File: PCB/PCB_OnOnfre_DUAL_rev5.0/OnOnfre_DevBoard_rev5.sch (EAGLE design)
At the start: 30 parts, among them J3Y S8050, J7 8p, K1 OMRON-G3MB-202P-SSR2, K2 OMRON-G3MB-202P-SSR2, U2 esp12

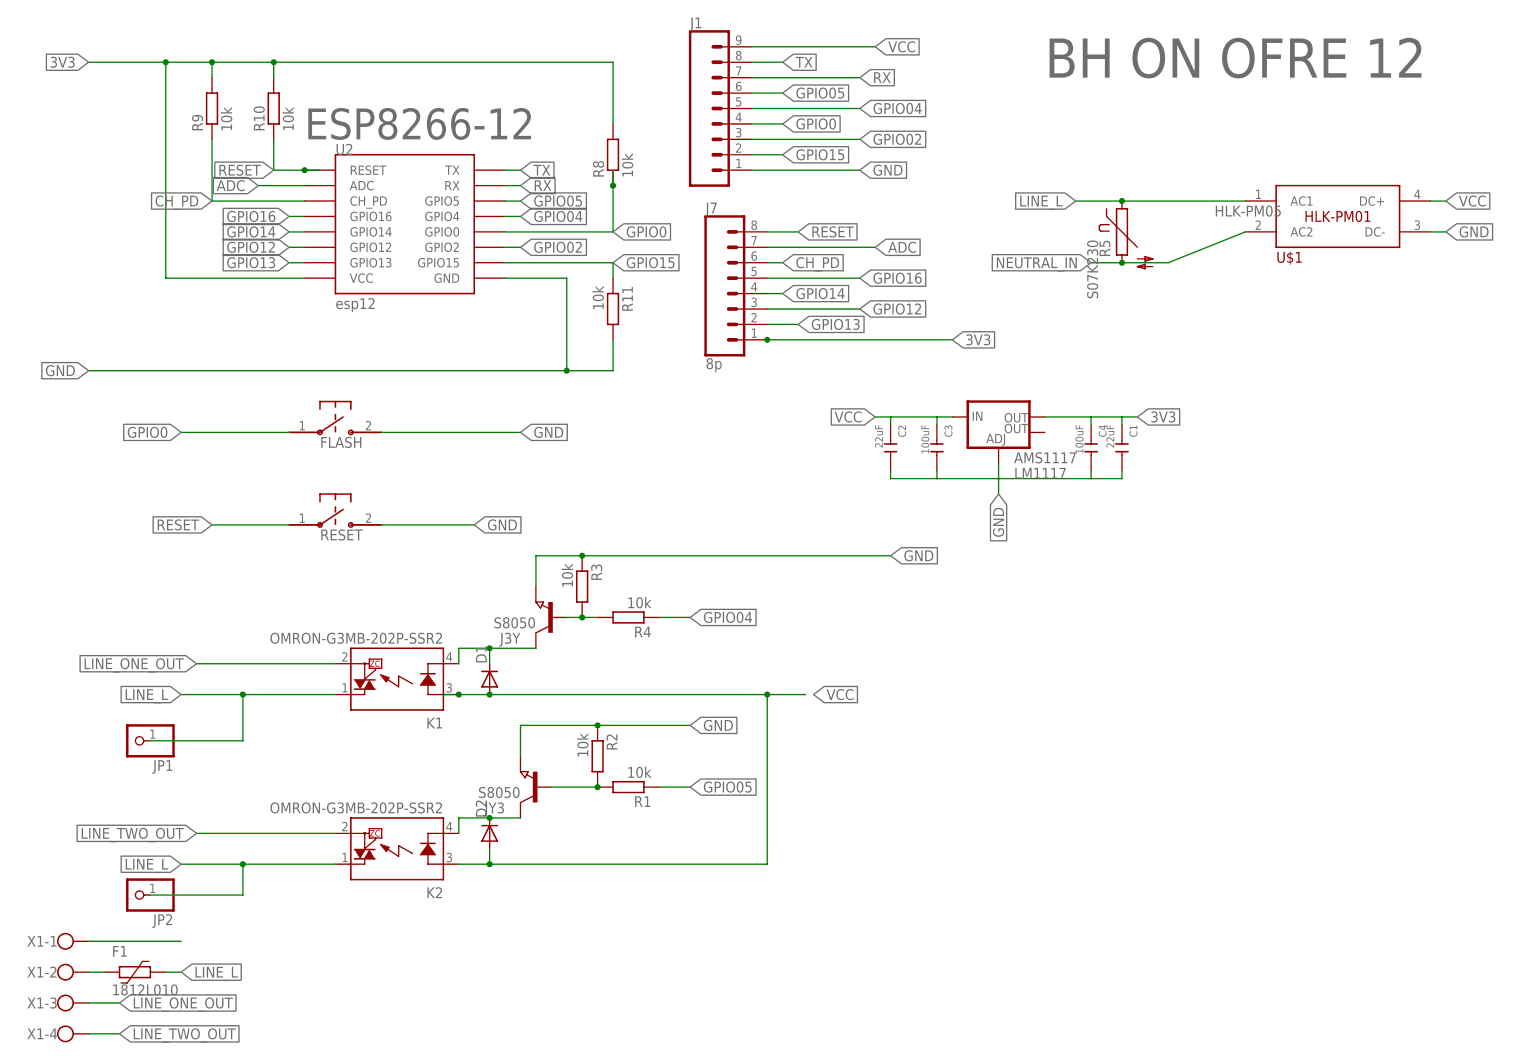
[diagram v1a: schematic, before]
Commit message: rev5 adc A0
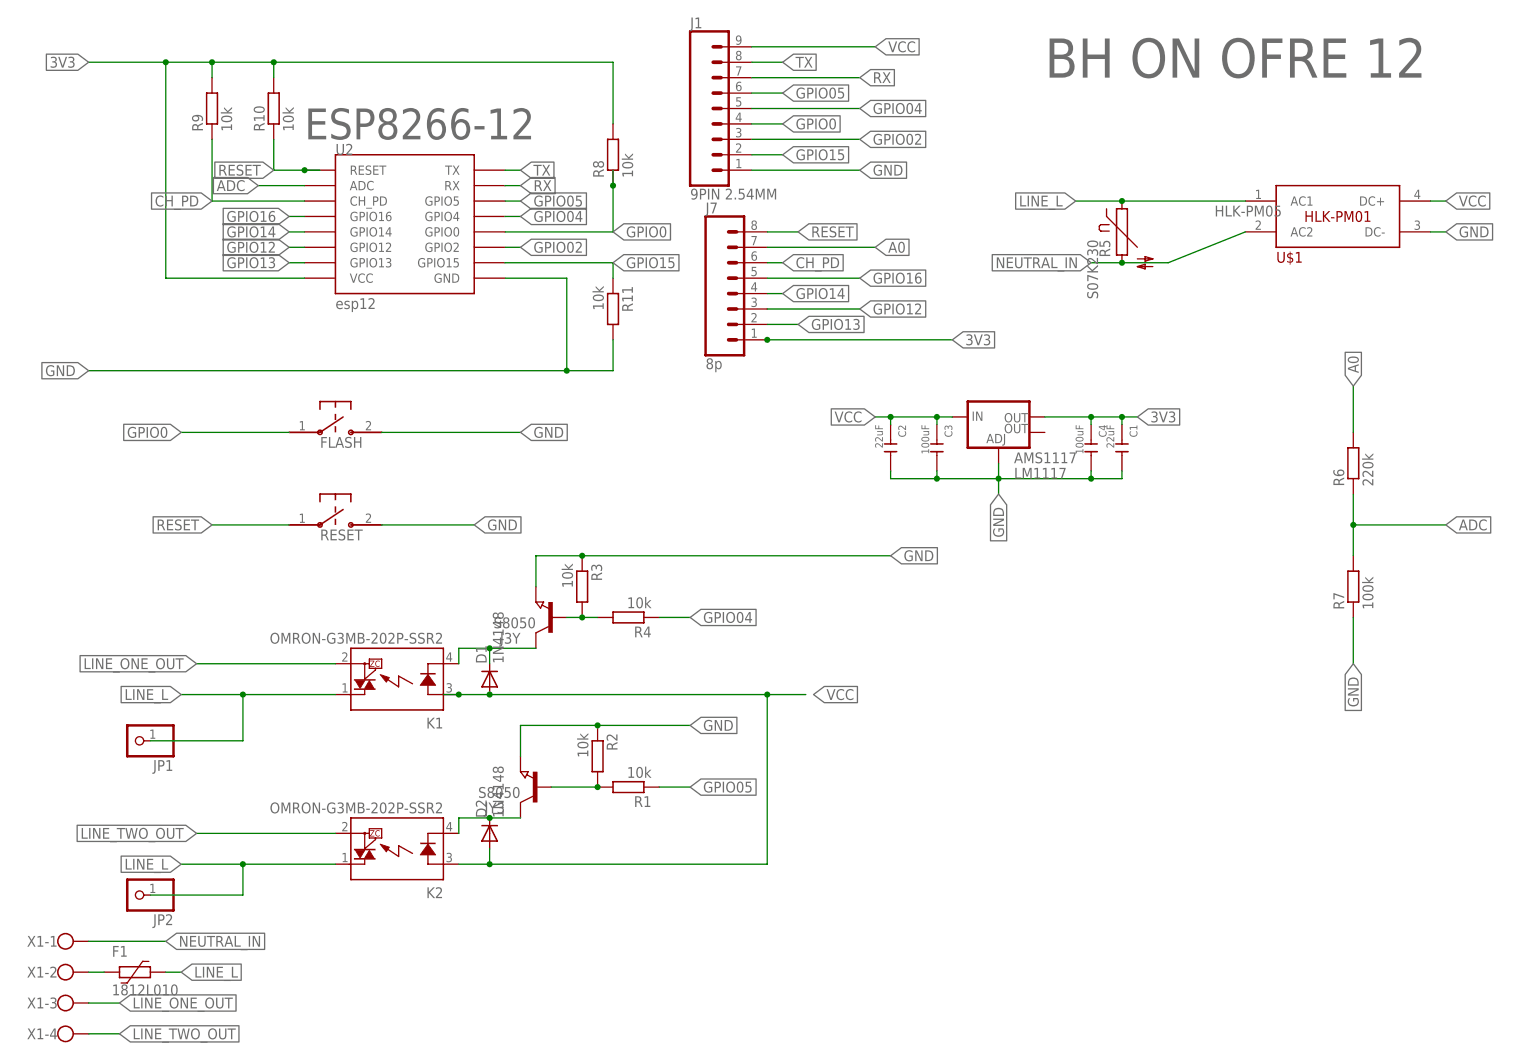
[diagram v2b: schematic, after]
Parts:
- added R6: 220k, resistor:R-EU_R0603
- added R7: 100k, resistor:R-EU_R0603
- D1, D2: value (none) -> 1N4148
- J1: value (none) -> 9PIN 2.54MM
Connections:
- new net A0: J7.7, R6.2
- net ADC: now also R6.1, R7.2; no longer J7.7
- net GND: now also R7.1
